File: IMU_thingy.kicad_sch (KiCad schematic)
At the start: 7 parts, among them U1 BNO055

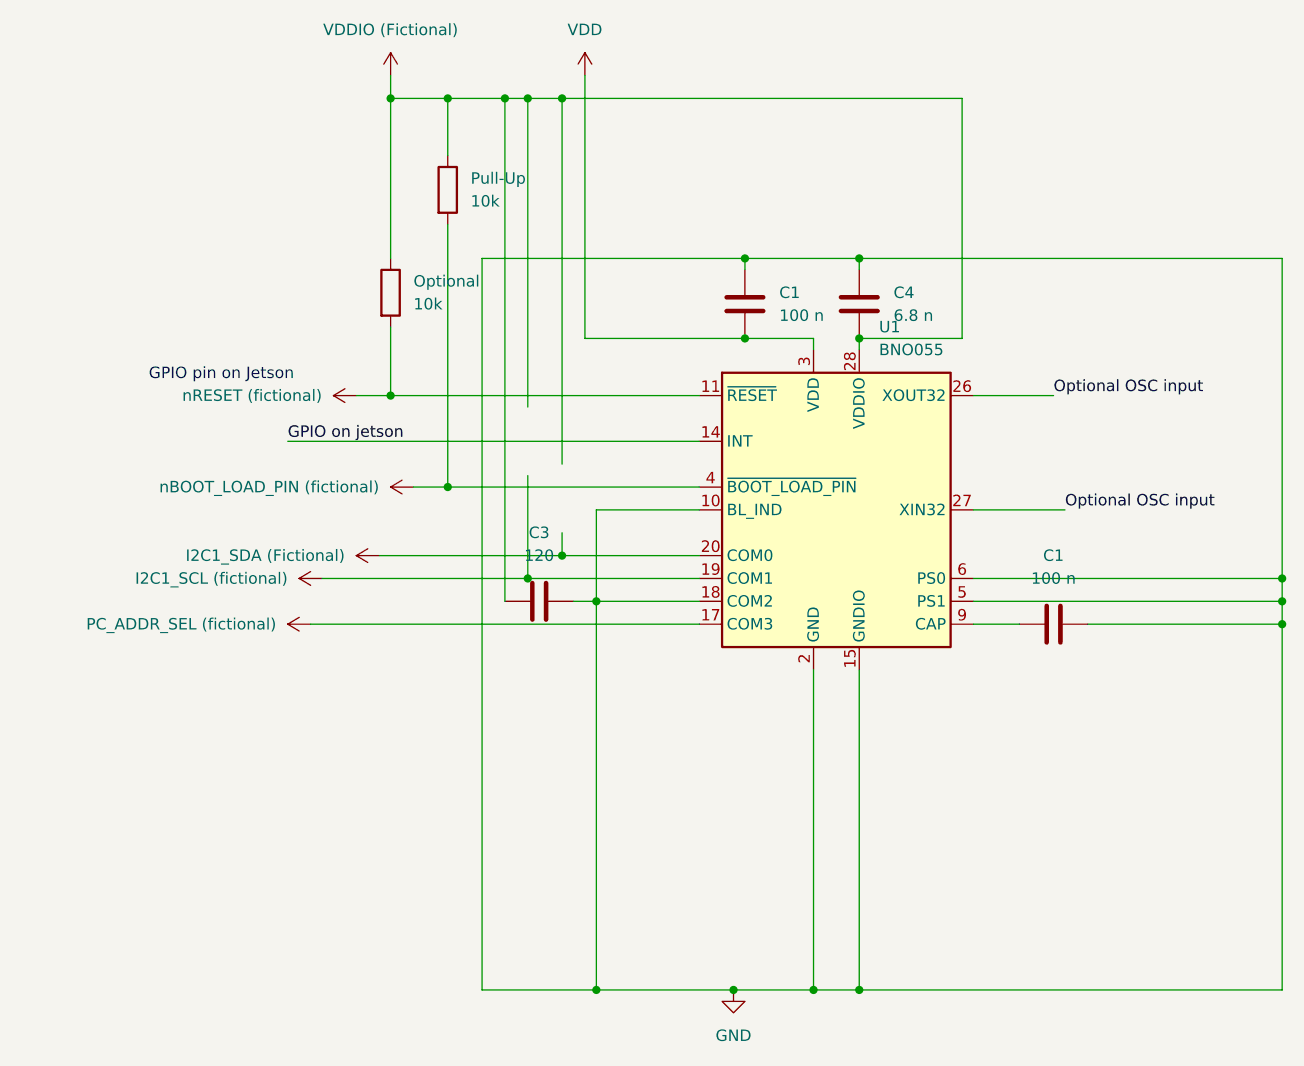
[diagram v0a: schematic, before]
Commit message: IMU Subcircuit (revised1)
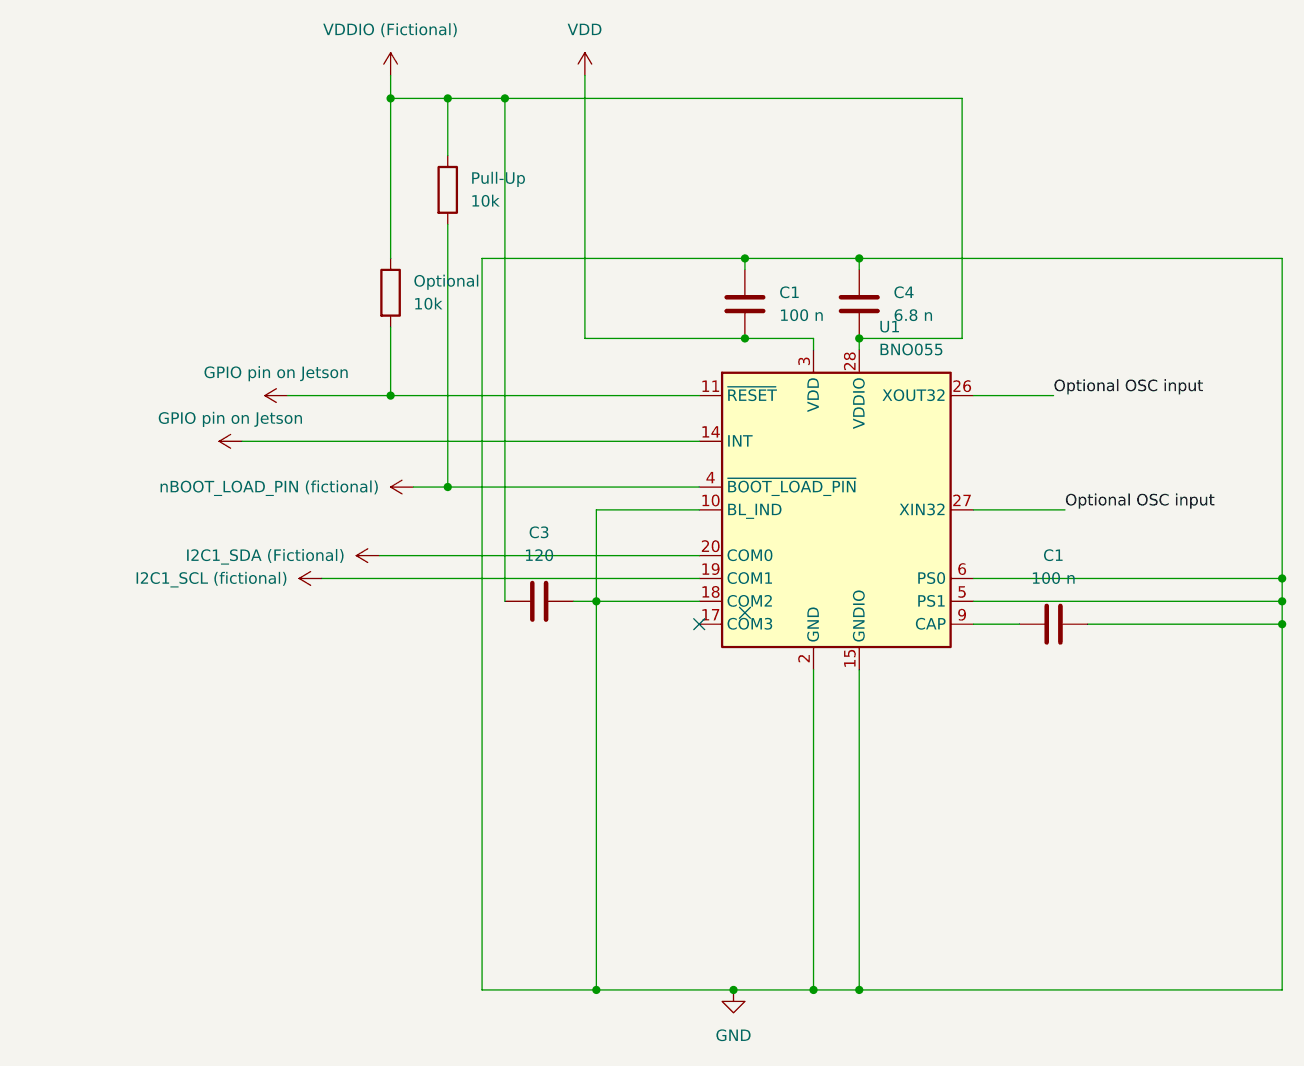
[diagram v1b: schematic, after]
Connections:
- net nRESET (fictional) is gone; now on net GPIO pin on Jetson: Optional.2, U1.11 (~{RESET})
- net GPIO  on jetson renamed GPIO pin on Jetson
- net PC_ADDR_SEL (fictional): no longer names the net of U1.17 (COM3)
- no-connect marks 0 -> 2
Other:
- note removed: "GPIO pin on Jetson"
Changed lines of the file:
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@@
-	)
-	(junction
-		(at 67.31 74.93)
-		(diameter 0)
-		(color 0 0 0 0)
 	)
 	(junction
@@
 	)
 	(junction
-		(at 71.12 72.39)
-		(diameter 0)
-		(color 0 0 0 0)
-	)
-	(junction
 		(at 58.42 21.59)
 		(diameter 0)
@@
 	)
 	(junction
-		(at 71.12 21.59)
-		(diameter 0)
-		(color 0 0 0 0)
-	)
-	(junction
 		(at 99.06 120.65)
 		(diameter 0)
@@
 		(color 0 0 0 0)
 	)
-	(junction
-		(at 67.31 21.59)
-		(diameter 0)
-		(color 0 0 0 0)
+	(no_connect
+		(at 86.36 80.01)
+	)
+	(no_connect
+		(at 91.44 78.74)
 	)
 	(wire
@@
 	(wire
 		(pts
-			(xy 71.12 69.85) (xy 71.12 72.39)
-		)
-		(stroke
-			(width 0)
-			(type default)
-		)
-	)
-	(wire
-		(pts
-			(xy 71.12 21.59) (xy 71.12 62.23)
-		)
-		(stroke
-			(width 0)
-			(type default)
-		)
-	)
-	(wire
-		(pts
 			(xy 64.77 21.59) (xy 64.77 77.47)
 		)
@@
 	(wire
 		(pts
-			(xy 43.18 80.01) (xy 86.36 80.01)
-		)
-		(stroke
-			(width 0)
-			(type default)
-		)
-	)
-	(wire
-		(pts
 			(xy 116.84 77.47) (xy 151.13 77.47)
 		)
@@
 	(wire
 		(pts
+			(xy 35.56 59.69) (xy 86.36 59.69)
+		)
+		(stroke
+			(width 0)
+			(type default)
+		)
+	)
+	(wire
+		(pts
 			(xy 151.13 74.93) (xy 151.13 77.47)
 		)
@@
 	(wire
 		(pts
-			(xy 52.07 54.61) (xy 48.26 54.61)
+			(xy 52.07 54.61) (xy 40.64 54.61)
 		)
 		(stroke
@@
 	(wire
 		(pts
-			(xy 67.31 63.5) (xy 67.31 74.93)
-		)
-		(stroke
-			(width 0)
-			(type default)
-		)
-	)
-	(wire
-		(pts
 			(xy 104.14 39.37) (xy 151.13 39.37)
 		)
@@
 	(wire
 		(pts
-			(xy 71.12 72.39) (xy 86.36 72.39)
-		)
-		(stroke
-			(width 0)
-			(type default)
-		)
-	)
-	(wire
-		(pts
-			(xy 67.31 74.93) (xy 86.36 74.93)
+			(xy 50.8 72.39) (xy 86.36 72.39)
 		)
 		(stroke
@@
 	(wire
 		(pts
-			(xy 64.77 21.59) (xy 67.31 21.59)
-		)
-		(stroke
-			(width 0)
-			(type default)
-		)
-	)
-	(wire
-		(pts
 			(xy 62.23 39.37) (xy 62.23 120.65)
 		)
@@
 	(wire
 		(pts
-			(xy 71.12 21.59) (xy 115.57 21.59)
-		)
-		(stroke
-			(width 0)
-			(type default)
-		)
-	)
-	(wire
-		(pts
 			(xy 104.14 85.09) (xy 104.14 120.65)
 		)
@@
 	(wire
 		(pts
-			(xy 44.45 74.93) (xy 67.31 74.93)
+			(xy 44.45 74.93) (xy 86.36 74.93)
 		)
 		(stroke
@@
 	(wire
 		(pts
-			(xy 50.8 72.39) (xy 71.12 72.39)
-		)
-		(stroke
-			(width 0)
-			(type default)
-		)
-	)
-	(wire
-		(pts
 			(xy 104.14 48.26) (xy 115.57 48.26)
 		)
@@
 	(wire
 		(pts
-			(xy 40.64 59.69) (xy 86.36 59.69)
-		)
-		(stroke
-			(width 0)
-			(type default)
-		)
-	)
-	(wire
-		(pts
-			(xy 67.31 21.59) (xy 67.31 55.88)
-		)
-		(stroke
-			(width 0)
-			(type default)
-		)
-	)
-	(wire
-		(pts
 			(xy 74.93 120.65) (xy 90.17 120.65)
 		)
@@
 	(wire
 		(pts
-			(xy 67.31 21.59) (xy 71.12 21.59)
+			(xy 64.77 21.59) (xy 115.57 21.59)
 		)
 		(stroke
@@
 			(width 0)
 			(type default)
-		)
-	)
-	(text "GPIO pin on Jetson\n"
-		(exclude_from_sim no)
-		(at 33.274 52.324 0)
-		(effects
-			(font
-				(size 1.27 1.27)
-			)
-		)
-	)
-	(label "GPIO  on jetson"
-		(at 40.64 59.69 0)
-		(fields_autoplaced yes)
-		(effects
-			(font
-				(size 1.27 1.27)
-			)
-			(justify left bottom)
 		)
 	)
@@
 	(symbol
 		(lib_id "power:VDD")
-		(at 48.26 54.61 90)
+		(at 40.64 54.61 90)
 		(unit 1)
 		(exclude_from_sim no)
@@
 		(fields_autoplaced yes)
 		(property "Reference" "#PWR04"
-			(at 52.07 54.61 0)
-			(effects
-				(font
-					(size 1.27 1.27)
-				)
-				(hide yes)
-			)
-		)
-		(property "Value" "nRESET (fictional)"
-			(at 44.45 54.6099 90)
-			(effects
-				(font
-					(size 1.27 1.27)
-				)
-				(justify left)
+			(at 44.45 54.61 0)
+			(effects
+				(font
+					(size 1.27 1.27)
+				)
+				(hide yes)
+			)
+		)
+		(property "Value" "GPIO pin on Jetson"
+			(at 39.37 52.07 90)
+			(effects
+				(font
+					(size 1.27 1.27)
+				)
 			)
 		)
 		(property "Footprint" ""
-			(at 48.26 54.61 0)
+			(at 40.64 54.61 0)
 			(effects
 				(font
@@
 		)
 		(property "Datasheet" ""
-			(at 48.26 54.61 0)
+			(at 40.64 54.61 0)
 			(effects
 				(font
@@
 		)
 		(property "Description" "Power symbol creates a global label with name \"VDD\""
-			(at 48.26 54.61 0)
+			(at 40.64 54.61 0)
 			(effects
 				(font
@@
 	(symbol
 		(lib_id "power:VDD")
-		(at 43.18 80.01 90)
+		(at 35.56 59.69 90)
 		(unit 1)
 		(exclude_from_sim no)
@@
 		(dnp no)
 		(fields_autoplaced yes)
-		(property "Reference" "#PWR08"
-			(at 46.99 80.01 0)
-			(effects
-				(font
-					(size 1.27 1.27)
-				)
-				(hide yes)
-			)
-		)
-		(property "Value" "PC_ADDR_SEL (fictional)"
-			(at 39.37 80.0099 90)
-			(effects
-				(font
-					(size 1.27 1.27)
-				)
-				(justify left)
+		(property "Reference" "#PWR09"
+			(at 39.37 59.69 0)
+			(effects
+				(font
+					(size 1.27 1.27)
+				)
+				(hide yes)
+			)
+		)
+		(property "Value" "GPIO pin on Jetson"
+			(at 34.29 57.15 90)
+			(effects
+				(font
+					(size 1.27 1.27)
+				)
 			)
 		)
 		(property "Footprint" ""
-			(at 43.18 80.01 0)
+			(at 35.56 59.69 0)
 			(effects
 				(font
@@
 		)
 		(property "Datasheet" ""
-			(at 43.18 80.01 0)
+			(at 35.56 59.69 0)
 			(effects
 				(font
@@
 		)
 		(property "Description" "Power symbol creates a global label with name \"VDD\""
-			(at 43.18 80.01 0)
+			(at 35.56 59.69 0)
 			(effects
 				(font
@@
 		)
 		(instances
-			(project "First"
+			(project "IMU_thingy"
 				(path "/410c1f18-3e74-48a2-a221-f677648ccabd"
-					(reference "#PWR08")
+					(reference "#PWR09")
 					(unit 1)
 				)

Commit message: IMU Subcircuit (revised 2)
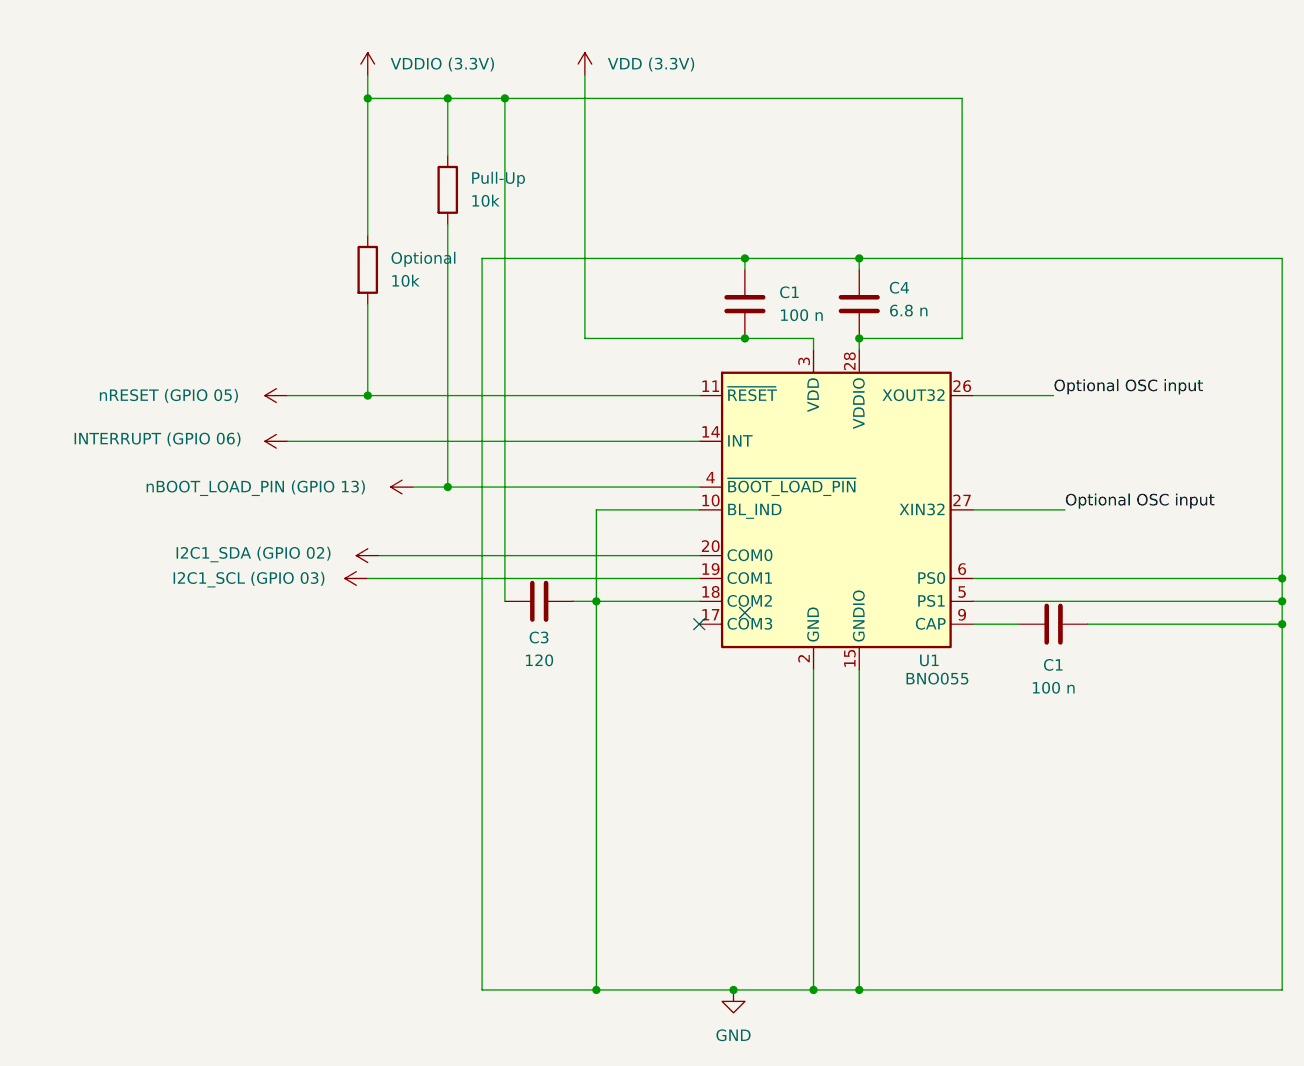
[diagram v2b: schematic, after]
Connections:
- net GPIO pin on Jetson renamed nRESET (GPIO 05)
- net nRESET (GPIO 05): no longer U1.14 (INT)
- net I2C1_SCL (fictional) renamed I2C1_SCL (GPIO 03)
- net I2C1_SDA (Fictional) renamed I2C1_SDA (GPIO 02)
- net VDD renamed VDD (3.3V)
- net VDDIO (Fictional) renamed VDDIO (3.3V)
- net nBOOT_LOAD_PIN (fictional) renamed nBOOT_LOAD_PIN (GPIO 13)
- new net INTERRUPT (GPIO 06): U1.14 (INT)
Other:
- moved on the sheet: Optional

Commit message: With Footprints done now
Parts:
- C1, C3, C4: footprint (none) -> Capacitor_SMD:CP_Elec_4x3
- C2: renamed from C1; footprint (none) -> Capacitor_SMD:CP_Elec_4x3
- Optional1: renamed from Optional; footprint (none) -> Resistor_SMD:R_0603_1608Metric_Pad0.98x0.95mm_HandSolder
- Pull-Up1: renamed from Pull-Up; footprint (none) -> Resistor_SMD:R_0603_1608Metric_Pad0.98x0.95mm_HandSolder
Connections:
- net COM3 (GPIO 19): now reaches U1.17 (COM3)
- net Optional OSC input: no longer names the net of U1.26 (XOUT32)
- net Optional OSC input: no longer U1.27 (XIN32)
- no-connect marks 2 -> 3
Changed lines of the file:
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@@
 	)
 	(no_connect
-		(at 86.36 80.01)
+		(at 116.84 67.31)
 	)
 	(no_connect
 		(at 91.44 78.74)
 	)
+	(no_connect
+		(at 116.84 54.61)
+	)
 	(wire
 		(pts
@@
 	(wire
 		(pts
+			(xy 86.36 91.44) (xy 53.34 91.44)
+		)
+		(stroke
+			(width 0)
+			(type default)
+		)
+	)
+	(wire
+		(pts
 			(xy 99.06 120.65) (xy 104.14 120.65)
 		)
@@
 	(wire
 		(pts
-			(xy 116.84 67.31) (xy 127 67.31)
-		)
-		(stroke
-			(width 0)
-			(type default)
-		)
-	)
-	(wire
-		(pts
 			(xy 62.23 39.37) (xy 91.44 39.37)
 		)
@@
 	(wire
 		(pts
-			(xy 116.84 54.61) (xy 125.73 54.61)
-		)
-		(stroke
-			(width 0)
-			(type default)
-		)
-	)
-	(wire
-		(pts
 			(xy 104.14 39.37) (xy 151.13 39.37)
 		)
@@
 	(wire
 		(pts
+			(xy 86.36 80.01) (xy 86.36 91.44)
+		)
+		(stroke
+			(width 0)
+			(type default)
+		)
+	)
+	(wire
+		(pts
 			(xy 74.93 120.65) (xy 90.17 120.65)
 		)
@@
 			(width 0)
 			(type default)
-		)
-	)
-	(label "Optional OSC input"
-		(at 127 67.31 0)
-		(fields_autoplaced yes)
-		(effects
-			(font
-				(size 1.27 1.27)
-			)
-			(justify left bottom)
-		)
-	)
-	(label "Optional OSC input"
-		(at 125.73 54.61 0)
-		(fields_autoplaced yes)
-		(effects
-			(font
-				(size 1.27 1.27)
-			)
-			(justify left bottom)
 		)
 	)
@@
 			)
 		)
-		(property "Footprint" ""
+		(property "Footprint" "Capacitor_SMD:CP_Elec_4x3"
 			(at 92.4052 48.26 0)
 			(effects
@@
 		(on_board yes)
 		(dnp no)
-		(property "Reference" "C1"
+		(property "Reference" "C2"
 			(at 125.73 84.582 90)
 			(effects
@@
 			)
 		)
-		(property "Footprint" ""
+		(property "Footprint" "Capacitor_SMD:CP_Elec_4x3"
 			(at 129.54 79.0448 0)
 			(effects
@@
 			(project ""
 				(path "/410c1f18-3e74-48a2-a221-f677648ccabd"
-					(reference "C1")
+					(reference "C2")
 					(unit 1)
 				)
@@
 			)
 		)
-		(property "Footprint" ""
+		(property "Footprint" "Capacitor_SMD:CP_Elec_4x3"
 			(at 105.1052 48.26 0)
 			(effects
@@
 			)
 		)
-		(property "Footprint" ""
+		(property "Footprint" "Capacitor_SMD:CP_Elec_4x3"
 			(at 64.77 78.4352 0)
 			(effects
@@
 		(dnp no)
 		(fields_autoplaced yes)
-		(property "Reference" "Optional"
+		(property "Reference" "Optional1"
 			(at 52.07 39.3699 0)
 			(effects
@@
 			)
 		)
-		(property "Footprint" ""
+		(property "Footprint" "Resistor_SMD:R_0603_1608Metric_Pad0.98x0.95mm_HandSolder"
 			(at 47.752 40.64 90)
 			(effects
@@
 			(project ""
 				(path "/410c1f18-3e74-48a2-a221-f677648ccabd"
-					(reference "Optional")
+					(reference "Optional1")
 					(unit 1)
 				)
@@
 		(dnp no)
 		(fields_autoplaced yes)
-		(property "Reference" "Pull-Up"
+		(property "Reference" "Pull-Up1"
 			(at 60.96 30.4799 0)
 			(effects
@@
 			)
 		)
-		(property "Footprint" ""
+		(property "Footprint" "Resistor_SMD:R_0603_1608Metric_Pad0.98x0.95mm_HandSolder"
 			(at 56.642 31.75 90)
 			(effects
@@
 			(project ""
 				(path "/410c1f18-3e74-48a2-a221-f677648ccabd"
-					(reference "Pull-Up")
+					(reference "Pull-Up1")
 					(unit 1)
 				)
+			)
+		)
+	)
+	(symbol
+		(lib_id "power:VDD")
+		(at 53.34 91.44 90)
+		(unit 1)
+		(exclude_from_sim no)
+		(in_bom yes)
+		(on_board yes)
+		(dnp no)
+		(property "Reference" "#PWR08"
+			(at 57.15 91.44 0)
+			(effects
+				(font
+					(size 1.27 1.27)
+				)
+				(hide yes)
+			)
+		)
+		(property "Value" "COM3 (GPIO 19)"
+			(at 40.132 91.44 90)
+			(effects
+				(font
+					(size 1.27 1.27)
+				)
+			)
+		)
+		(property "Footprint" ""
+			(at 53.34 91.44 0)
+			(effects
+				(font
+					(size 1.27 1.27)
+				)
+				(hide yes)
+			)
+		)
+		(property "Datasheet" ""
+			(at 53.34 91.44 0)
+			(effects
+				(font
+					(size 1.27 1.27)
+				)
+				(hide yes)
+			)
+		)
+		(property "Description" "Power symbol creates a global label with name \"VDD\""
+			(at 53.34 91.44 0)
+			(effects
+				(font
+					(size 1.27 1.27)
+				)
+				(hide yes)
+			)
+		)
+		(pin "1"
+		)
+		(instances
+			(project "IMU_thingy"
+				(path "/410c1f18-3e74-48a2-a221-f677648ccabd"
+					(reference "#PWR08")
+					(unit 1)
+				)
